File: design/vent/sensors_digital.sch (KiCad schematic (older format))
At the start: 13 parts, among them Q1 Q_NMOS_GSD, Q2 Q_NMOS_GSD, U6 LP2980AIM5-3.0, U7 LSM6DS3HTR, U8 BMG250, U9 MS5607-02BA03

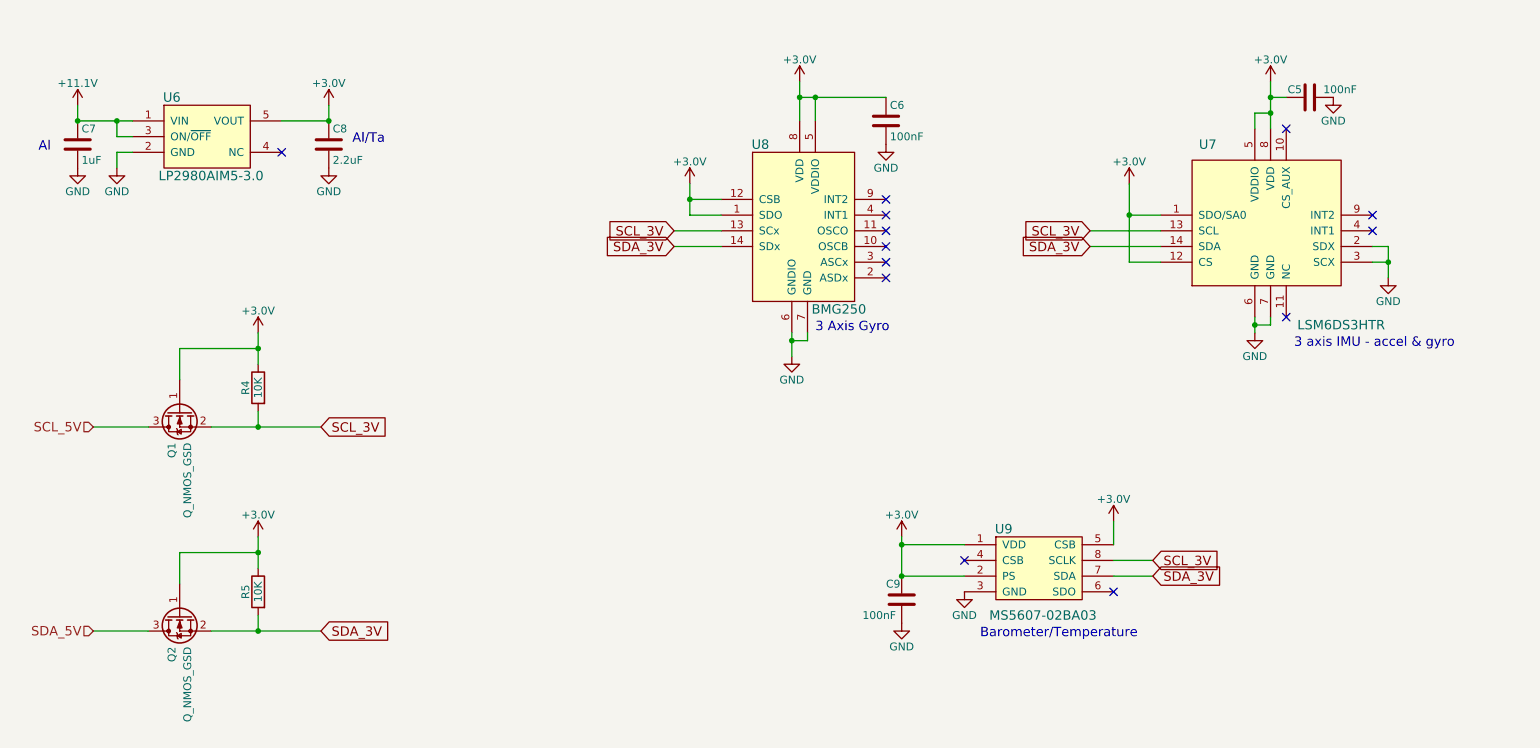
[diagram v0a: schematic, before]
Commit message: Refine schematic
- Add part numbers and correct pinout for mosfets
- Add fuses to battery inputs
- Add decoupling caps to logic translators
- Add flyback diodes to H Bridge, to be populated if the body diodes of
  the mosfets are not sufficient.
- Change H Bridge to operate with 4 inputs instead of 2.

Also, misc directory cleanup.
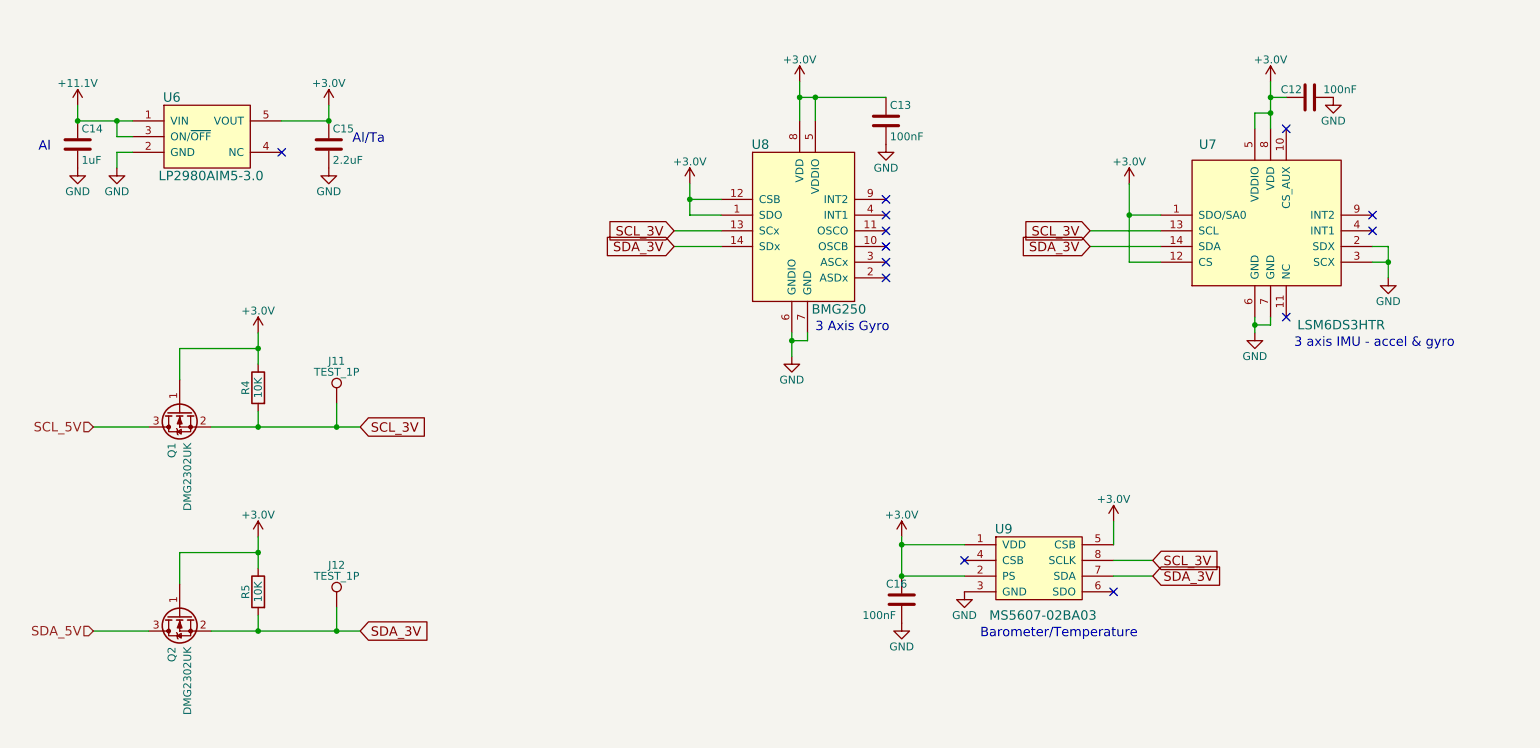
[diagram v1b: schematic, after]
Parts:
- added J11, J12: TEST_1P, symbol TEST_1P
- Q1, Q2: value Q_NMOS_GSD -> DMG2302UK
- renumbered C5 to C12, C6 to C13, C7 to C14, C8 to C15, C9 to C16
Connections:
- net SCL_3V: now also J11.1
- net SDA_3V: now also J12.1
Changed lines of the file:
@@
 $EndComp
 $Comp
-L GND #PWR46
+L GND #PWR53
 U 1 1 5AE13B89
 P 9100 3400
-F 0 "#PWR46" H 9100 3150 50  0001 C CNN
+F 0 "#PWR53" H 9100 3150 50  0001 C CNN
 F 1 "GND" H 9100 3250 50  0000 C CNN
 F 2 "" H 9100 3400 50  0001 C CNN
@@
 NoConn ~ 9300 2100
 $Comp
-L +3.0V #PWR34
+L +3.0V #PWR41
 U 1 1 5AE13B91
 P 9200 1800
-F 0 "#PWR34" H 9200 1650 50  0001 C CNN
+F 0 "#PWR41" H 9200 1650 50  0001 C CNN
 F 1 "+3.0V" H 9200 1940 50  0000 C CNN
 F 2 "" H 9200 1800 50  0001 C CNN
@@
 $EndComp
 $Comp
-L C C5
+L C C12
 U 1 1 5AE13B97
 P 9450 1900
-F 0 "C5" V 9500 1950 50  0000 L CNN
+F 0 "C12" V 9500 1950 50  0000 L CNN
 F 1 "100nF" V 9500 1600 50  0000 L CNN
 F 2 "Capacitors_SMD:C_0603_HandSoldering" H 9488 1750 50  0001 C CNN
@@
 $EndComp
 $Comp
-L GND #PWR35
+L GND #PWR42
 U 1 1 5AE13B9E
 P 9600 1900
-F 0 "#PWR35" H 9600 1650 50  0001 C CNN
+F 0 "#PWR42" H 9600 1650 50  0001 C CNN
 F 1 "GND" H 9600 1750 50  0000 C CNN
 F 2 "" H 9600 1900 50  0001 C CNN
@@
 $EndComp
 $Comp
-L GND #PWR44
+L GND #PWR51
 U 1 1 5AE13BA4
 P 9950 3050
-F 0 "#PWR44" H 9950 2800 50  0001 C CNN
+F 0 "#PWR51" H 9950 2800 50  0001 C CNN
 F 1 "GND" H 9950 2900 50  0000 C CNN
 F 2 "" H 9950 3050 50  0001 C CNN
@@
 NoConn ~ 8200 5050
 $Comp
-L C C9
+L C C16
 U 1 1 5AE13BC4
 P 6850 5100
-F 0 "C9" H 6750 5200 50  0000 L CNN
+F 0 "C16" H 6750 5200 50  0000 L CNN
 F 1 "100nF" H 6600 5000 50  0000 L CNN
 F 2 "Capacitors_SMD:C_0603_HandSoldering" H 6888 4950 50  0001 C CNN
@@
 $EndComp
 $Comp
-L +3.0V #PWR50
+L +3.0V #PWR57
 U 1 1 5AE13BCB
 P 6850 4700
-F 0 "#PWR50" H 6850 4550 50  0001 C CNN
+F 0 "#PWR57" H 6850 4550 50  0001 C CNN
 F 1 "+3.0V" H 6850 4840 50  0000 C CNN
 F 2 "" H 6850 4700 50  0001 C CNN
@@
 $EndComp
 $Comp
-L GND #PWR52
+L GND #PWR59
 U 1 1 5AE13BD1
 P 6850 5250
-F 0 "#PWR52" H 6850 5000 50  0001 C CNN
+F 0 "#PWR59" H 6850 5000 50  0001 C CNN
 F 1 "GND" H 6850 5100 50  0000 C CNN
 F 2 "" H 6850 5250 50  0001 C CNN
@@
 Barometer/Temperature
 $Comp
-L GND #PWR51
+L GND #PWR58
 U 1 1 5AE13C37
 P 7250 5050
-F 0 "#PWR51" H 7250 4800 50  0001 C CNN
+F 0 "#PWR58" H 7250 4800 50  0001 C CNN
 F 1 "GND" H 7250 4900 50  0000 C CNN
 F 2 "" H 7250 5050 50  0001 C CNN
@@
 SDA_3V
 $Comp
-L +3.0V #PWR43
+L +3.0V #PWR50
 U 1 1 5AE13CB0
 P 8300 2450
-F 0 "#PWR43" H 8300 2300 50  0001 C CNN
+F 0 "#PWR50" H 8300 2300 50  0001 C CNN
 F 1 "+3.0V" H 8300 2590 50  0000 C CNN
 F 2 "" H 8300 2450 50  0001 C CNN
@@
 $EndComp
 $Comp
-L +3.0V #PWR48
+L +3.0V #PWR55
 U 1 1 5AE13CD6
 P 8200 4600
-F 0 "#PWR48" H 8200 4450 50  0001 C CNN
+F 0 "#PWR55" H 8200 4450 50  0001 C CNN
 F 1 "+3.0V" H 8200 4740 50  0000 C CNN
 F 2 "" H 8200 4600 50  0001 C CNN
@@
 $EndComp
 $Comp
-L GND #PWR47
+L GND #PWR54
 U 1 1 5AE13CF8
 P 6150 3550
-F 0 "#PWR47" H 6150 3300 50  0001 C CNN
+F 0 "#PWR54" H 6150 3300 50  0001 C CNN
 F 1 "GND" H 6150 3400 50  0000 C CNN
 F 2 "" H 6150 3550 50  0001 C CNN
@@
 NoConn ~ 6750 3050
 $Comp
-L +3.0V #PWR33
+L +3.0V #PWR40
 U 1 1 5AE13D04
 P 6200 1800
-F 0 "#PWR33" H 6200 1650 50  0001 C CNN
+F 0 "#PWR40" H 6200 1650 50  0001 C CNN
 F 1 "+3.0V" H 6200 1940 50  0000 C CNN
 F 2 "" H 6200 1800 50  0001 C CNN
@@
 $EndComp
 $Comp
-L C C6
+L C C13
 U 1 1 5AE13D0A
 P 6750 2050
-F 0 "C6" H 6775 2150 50  0000 L CNN
+F 0 "C13" H 6775 2150 50  0000 L CNN
 F 1 "100nF" H 6775 1950 50  0000 L CNN
 F 2 "Capacitors_SMD:C_0603_HandSoldering" H 6788 1900 50  0001 C CNN
@@
 $EndComp
 $Comp
-L GND #PWR38
+L GND #PWR45
 U 1 1 5AE13D11
 P 6750 2200
-F 0 "#PWR38" H 6750 1950 50  0001 C CNN
+F 0 "#PWR45" H 6750 1950 50  0001 C CNN
 F 1 "GND" H 6750 2050 50  0000 C CNN
 F 2 "" H 6750 2200 50  0001 C CNN
@@
 $EndComp
 $Comp
-L +3.0V #PWR42
+L +3.0V #PWR49
 U 1 1 5AE13D7F
 P 5500 2450
-F 0 "#PWR42" H 5500 2300 50  0001 C CNN
+F 0 "#PWR49" H 5500 2300 50  0001 C CNN
 F 1 "+3.0V" H 5500 2590 50  0000 C CNN
 F 2 "" H 5500 2450 50  0001 C CNN
@@
 P 2250 3900
 F 0 "Q1" H 2450 3950 50  0000 L CNN
-F 1 "Q_NMOS_GSD" H 2450 3850 50  0000 L CNN
+F 1 "DMG2302UK" H 2450 3850 50  0000 L CNN
 F 2 "" H 2450 4000 50  0001 C CNN
 F 3 "" H 2250 3900 50  0001 C CNN
@@
 $EndComp
 $Comp
-L +3.0V #PWR45
+L +3.0V #PWR52
 U 1 1 5AE7CAE8
 P 2750 3400
-F 0 "#PWR45" H 2750 3250 50  0001 C CNN
+F 0 "#PWR52" H 2750 3250 50  0001 C CNN
 F 1 "+3.0V" H 2750 3540 50  0000 C CNN
 F 2 "" H 2750 3400 50  0001 C CNN
@@
 $EndComp
 Wire Wire Line
-	5500 2450 5500 2550
-Wire Wire Line
-	5500 2550 5500 2650
+	5500 2450 5500 2650
 Wire Wire Line
 	8200 4600 8200 4750
@@
 Connection ~ 6200 1900
 Wire Wire Line
-	6200 1900 6300 1900
-Wire Wire Line
-	6300 1900 6750 1900
-Wire Wire Line
-	6200 1800 6200 1900
-Wire Wire Line
-	6200 1900 6200 2050
+	6200 1900 6750 1900
+Wire Wire Line
+	6200 1800 6200 2050
 Connection ~ 6150 3450
 Wire Wire Line
@@
 	6250 3400 6250 3450
 Wire Wire Line
-	6150 3400 6150 3450
-Wire Wire Line
-	6150 3450 6150 3550
-Wire Wire Line
-	8300 2450 8300 2650
-Wire Wire Line
-	8300 2650 8300 2950
+	6150 3400 6150 3550
+Wire Wire Line
+	8300 2450 8300 2950
 Connection ~ 6850 4950
 Wire Wire Line
@@
 	7250 4750 6850 4750
 Wire Wire Line
-	6850 4700 6850 4750
-Wire Wire Line
-	6850 4750 6850 4950
+	6850 4700 6850 4950
 Wire Wire Line
 	8200 4950 8450 4950
@@
 	9950 2850 9850 2850
 Wire Wire Line
-	9950 2850 9950 2950
-Wire Wire Line
-	9950 2950 9950 3050
+	9950 2850 9950 3050
 Connection ~ 9200 1900
 Wire Wire Line
@@
 	9100 2000 9100 2100
 Wire Wire Line
-	9200 1800 9200 1900
-Wire Wire Line
-	9200 1900 9200 2000
-Wire Wire Line
-	9200 2000 9200 2100
+	9200 1800 9200 2100
 Connection ~ 9100 3350
 Wire Wire Line
@@
 	9200 3300 9200 3350
 Wire Wire Line
-	9100 3300 9100 3350
-Wire Wire Line
-	9100 3350 9100 3400
+	9100 3300 9100 3400
 Wire Wire Line
 	5500 2650 5700 2650
@@
 	2750 3900 2750 4000
 Wire Wire Line
-	2450 4000 2750 4000
-Wire Wire Line
-	2750 4000 3150 4000
-Wire Wire Line
-	2750 3400 2750 3500
-Wire Wire Line
-	2750 3500 2750 3600
+	2450 4000 3400 4000
+Wire Wire Line
+	2750 3400 2750 3600
 Wire Wire Line
 	2250 3700 2250 3500
@@
 	2250 3500 2750 3500
 Connection ~ 2750 3500
-Text GLabel 3150 4000 2    60   Input ~ 0
+Text GLabel 3400 4000 2    60   Input ~ 0
 SCL_3V
 Connection ~ 2750 4000
@@
 P 2250 5200
 F 0 "Q2" H 2450 5250 50  0000 L CNN
-F 1 "Q_NMOS_GSD" H 2450 5150 50  0000 L CNN
+F 1 "DMG2302UK" H 2450 5150 50  0000 L CNN
 F 2 "" H 2450 5300 50  0001 C CNN
 F 3 "" H 2250 5200 50  0001 C CNN
@@
 $EndComp
 $Comp
-L +3.0V #PWR49
+L +3.0V #PWR56
 U 1 1 5AE7D3E9
 P 2750 4700
-F 0 "#PWR49" H 2750 4550 50  0001 C CNN
+F 0 "#PWR56" H 2750 4550 50  0001 C CNN
 F 1 "+3.0V" H 2750 4840 50  0000 C CNN
 F 2 "" H 2750 4700 50  0001 C CNN
@@
 	2750 5200 2750 5300
 Wire Wire Line
-	2450 5300 2750 5300
-Wire Wire Line
-	2750 5300 3150 5300
-Wire Wire Line
-	2750 4700 2750 4800
-Wire Wire Line
-	2750 4800 2750 4900
+	2450 5300 3400 5300
+Wire Wire Line
+	2750 4700 2750 4900
 Wire Wire Line
 	2250 5000 2250 4800
@@
 	2250 4800 2750 4800
 Connection ~ 2750 4800
-Text GLabel 3150 5300 2    60   Input ~ 0
+Text GLabel 3400 5300 2    60   Input ~ 0
 SDA_3V
 Connection ~ 2750 5300
@@
 $EndComp
 $Comp
-L GND #PWR40
+L GND #PWR47
 U 1 1 5AE808B8
 P 1850 2350
-F 0 "#PWR40" H 1850 2100 50  0001 C CNN
+F 0 "#PWR47" H 1850 2100 50  0001 C CNN
 F 1 "GND" H 1850 2200 50  0000 C CNN
 F 2 "" H 1850 2350 50  0001 C CNN
@@
 $EndComp
 $Comp
-L C C7
+L C C14
 U 1 1 5AE808BE
 P 1600 2200
-F 0 "C7" H 1625 2300 50  0000 L CNN
+F 0 "C14" H 1625 2300 50  0000 L CNN
 F 1 "1uF" H 1625 2100 50  0000 L CNN
 F 2 "Capacitors_ThroughHole:CP_Radial_Tantal_D5.0mm_P2.50mm" H 1638 2050 50  0001 C CNN
@@
 $EndComp
 $Comp
-L GND #PWR39
+L GND #PWR46
 U 1 1 5AE808C5
 P 1600 2350
-F 0 "#PWR39" H 1600 2100 50  0001 C CNN
+F 0 "#PWR46" H 1600 2100 50  0001 C CNN
 F 1 "GND" H 1600 2200 50  0000 C CNN
 F 2 "" H 1600 2350 50  0001 C CNN
@@
 $EndComp
 $Comp
-L +3.0V #PWR37
+L +3.0V #PWR44
 U 1 1 5AE808CB
 P 3200 1950
-F 0 "#PWR37" H 3200 1800 50  0001 C CNN
+F 0 "#PWR44" H 3200 1800 50  0001 C CNN
 F 1 "+3.0V" H 3200 2090 50  0000 C CNN
 F 2 "" H 3200 1950 50  0001 C CNN
@@
 NoConn ~ 2900 2250
 $Comp
-L C C8
+L C C15
 U 1 1 5AE808D2
 P 3200 2200
-F 0 "C8" H 3225 2300 50  0000 L CNN
+F 0 "C15" H 3225 2300 50  0000 L CNN
 F 1 "2.2uF" H 3225 2100 50  0000 L CNN
 F 2 "Capacitors_ThroughHole:CP_Radial_Tantal_D5.0mm_P2.50mm" H 3238 2050 50  0001 C CNN
@@
 $EndComp
 $Comp
-L GND #PWR41
+L GND #PWR48
 U 1 1 5AE808D9
 P 3200 2350
-F 0 "#PWR41" H 3200 2100 50  0001 C CNN
+F 0 "#PWR48" H 3200 2100 50  0001 C CNN
 F 1 "GND" H 3200 2200 50  0000 C CNN
 F 2 "" H 3200 2350 50  0001 C CNN
@@
 	1600 1950 1600 2050
 Wire Wire Line
-	1600 2050 1850 2050
-Wire Wire Line
-	1850 2050 1950 2050
+	1600 2050 1950 2050
 Connection ~ 1600 2050
 Wire Wire Line
@@
 Connection ~ 3200 2050
 $Comp
-L +11.1V #PWR36
+L +11.1V #PWR43
 U 1 1 5AE808ED
 P 1600 1950
-F 0 "#PWR36" H 1600 1800 50  0001 C CNN
+F 0 "#PWR43" H 1600 1800 50  0001 C CNN
 F 1 "+11.1V" H 1600 2090 50  0000 C CNN
 F 2 "" H 1600 1950 50  0001 C CNN
@@
 Text HLabel 1700 5300 0    60   Input ~ 0
 SDA_5V
+$Comp
+L TEST_1P J11
+U 1 1 5AEBBCFA
+P 3250 3850
+F 0 "J11" H 3250 4120 50  0000 C CNN
+F 1 "TEST_1P" H 3250 4050 50  0000 C CNN
+F 2 "" H 3450 3850 50  0001 C CNN
+F 3 "" H 3450 3850 50  0001 C CNN
+	1    3250 3850
+	1    0    0    -1
+$EndComp
+$Comp
+L TEST_1P J12
+U 1 1 5AEBBD4E
+P 3250 5150
+F 0 "J12" H 3250 5420 50  0000 C CNN
+F 1 "TEST_1P" H 3250 5350 50  0000 C CNN
+F 2 "" H 3450 5150 50  0001 C CNN
+F 3 "" H 3450 5150 50  0001 C CNN
+	1    3250 5150
+	1    0    0    -1
+$EndComp
+Wire Wire Line
+	3250 3850 3250 4000
+Connection ~ 3250 4000
+Wire Wire Line
+	3250 5150 3250 5300
+Connection ~ 3250 5300
 $EndSCHEMATC

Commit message: Review changes
- Add debug LEDs
- Add pullup resistors on logic shifters for xbee and sd card.
- Add 0 ohm resistor between valve and control power sources (to allow
  for either one of both sources to be used).
- Add another IMU
- Add gate resistors to valve control mosfets
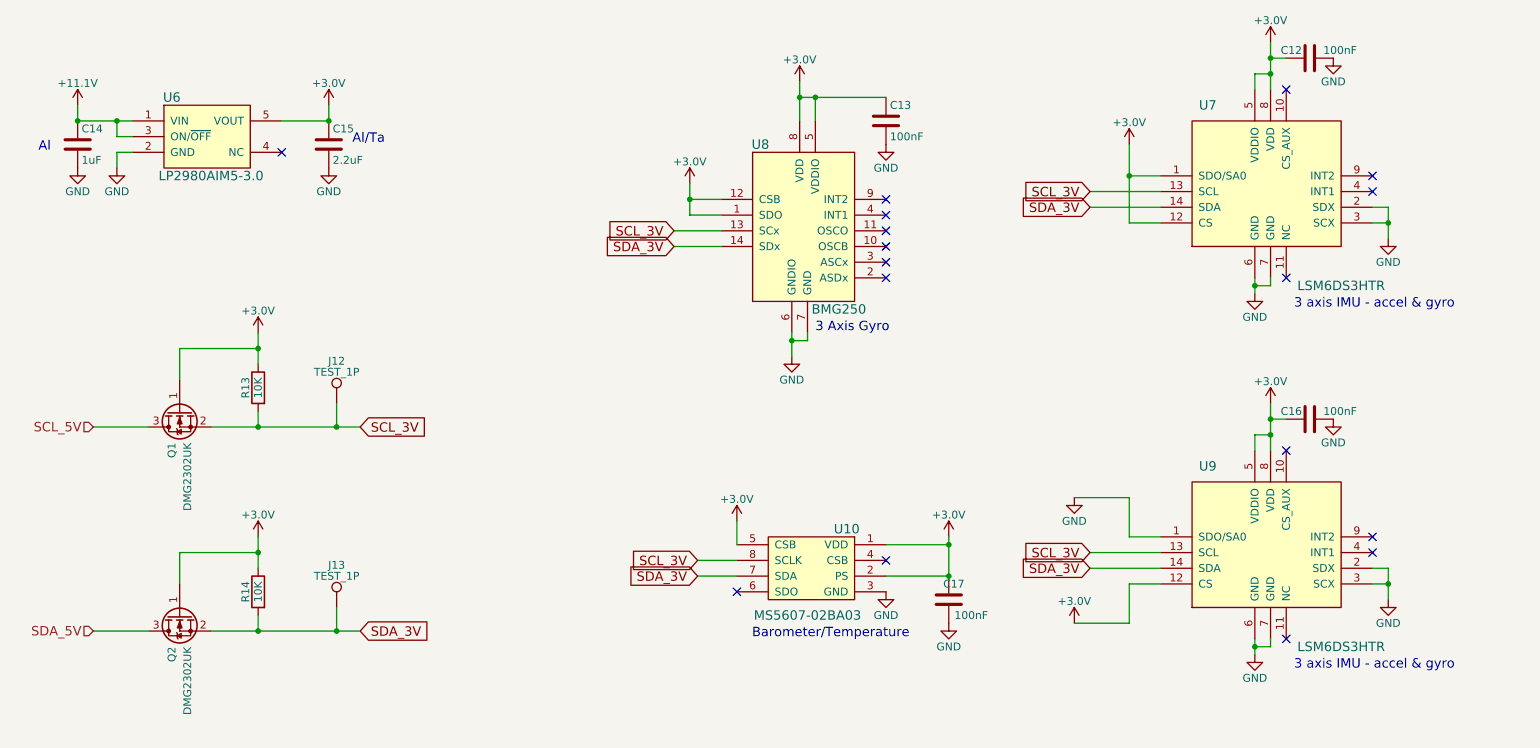
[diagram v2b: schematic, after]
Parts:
- added C16: 100nF, Capacitors_SMD:C_0603_HandSoldering, symbol C
- added U9: LSM6DS3HTR, LSM6DS3:PQFN50P300X250X86-14N, symbol LSM6DS3HTR
- renumbered C16 to C17, J11 to J12, J12 to J13, R4 to R13, R5 to R14, U9 to U10
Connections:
- net +3.0V: now also C16.1, U9.12 (CS), U9.5 (VDDIO), U9.8 (VDD)
- net GND: now also C16.2, U9.1 (SDO/SA0), U9.2 (SDX), U9.3 (SCX), U9.6 (GND), U9.7 (GND)
- net SCL_3V: now also U9.13 (SCL)
- net SDA_3V: now also U9.14 (SDA)
- no-connect marks 13 -> 17
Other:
- moved on the sheet: C12, C17, U10, U7

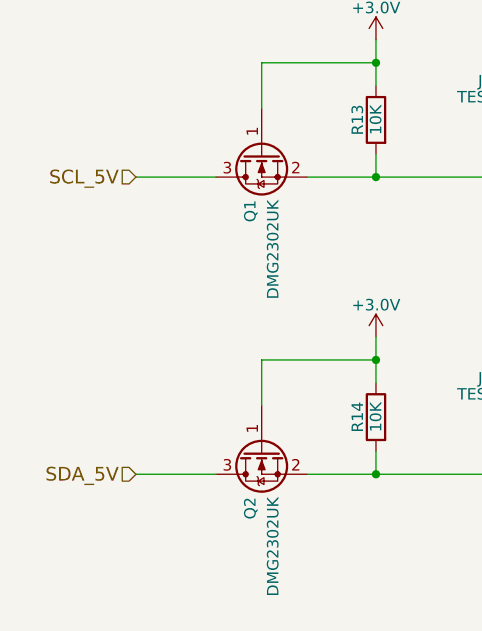
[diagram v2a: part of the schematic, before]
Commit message: Break out I2C lines on dsub connector
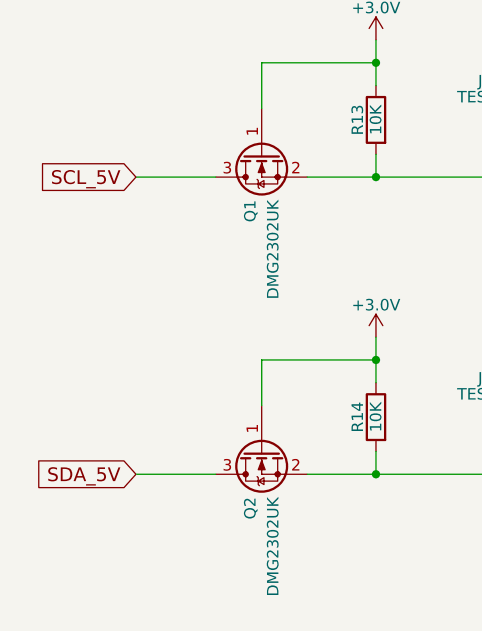
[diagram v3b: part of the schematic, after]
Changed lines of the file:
@@
 	1    0    0    -1
 $EndComp
-Text HLabel 1700 4000 0    60   Input ~ 0
-SCL_5V
-Text HLabel 1700 5300 0    60   Input ~ 0
-SDA_5V
 $Comp
 L TEST_1P J12
@@
 Wire Wire Line
 	8300 4450 8300 4700
+Text GLabel 1700 4000 0    60   Input ~ 0
+SCL_5V
+Text GLabel 1700 5300 0    60   Input ~ 0
+SDA_5V
 $EndSCHEMATC
